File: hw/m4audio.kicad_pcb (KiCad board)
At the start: 2 copper layers, 49.7 x 49.7 mm, 94 parts, among them J1 JACK_TRS, J11 CONN_01X03, J2 JACK_TRS, J21 CONN_01X03, P1 CONN_01X02, P2 USB_OTG, P3 CONN_02X05, P4 CONN_01X08, P5 CONN_01X03, P6 CONN_01X04, U1 LD1117S33TR, U2 STM32F405RG, U3 AD8542, U4 WM8731, Y1 Crystal

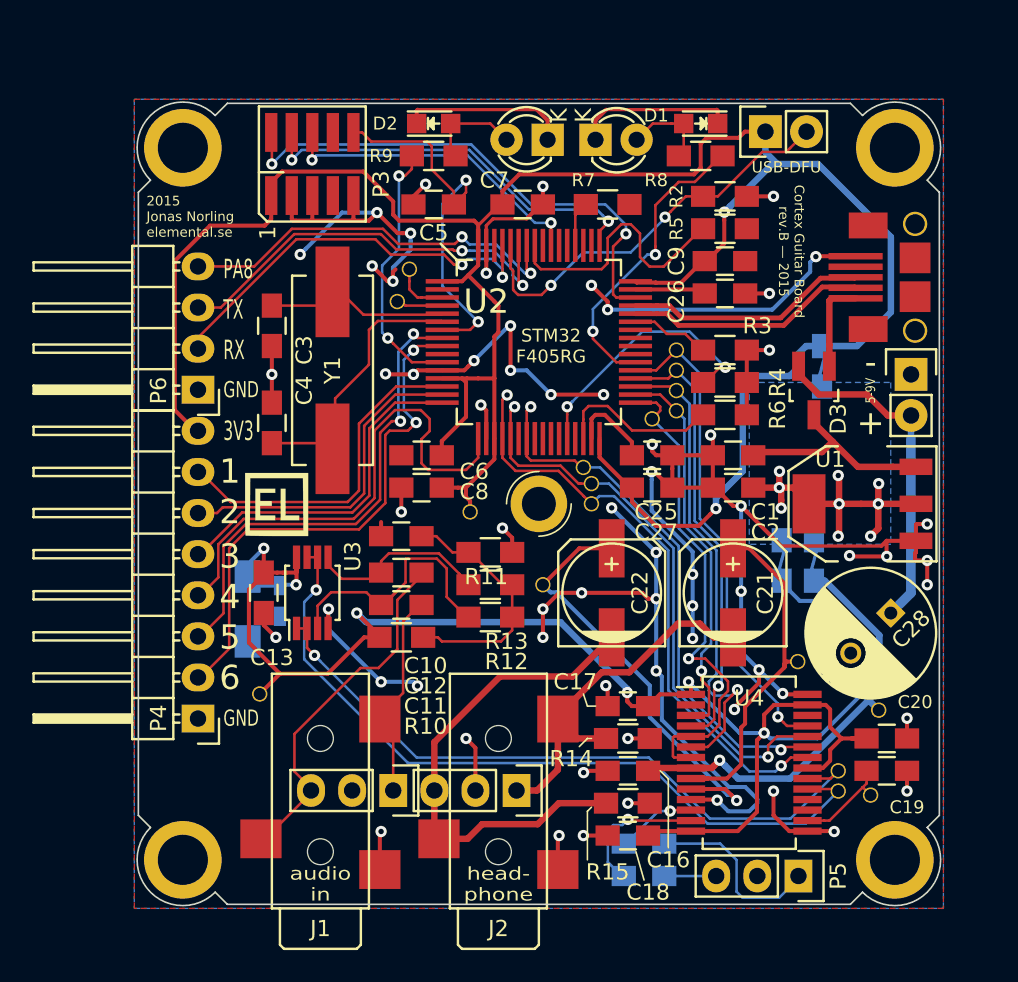
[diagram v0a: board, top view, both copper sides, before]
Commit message: Adjust testpoint drill and annular, for ITEAD production
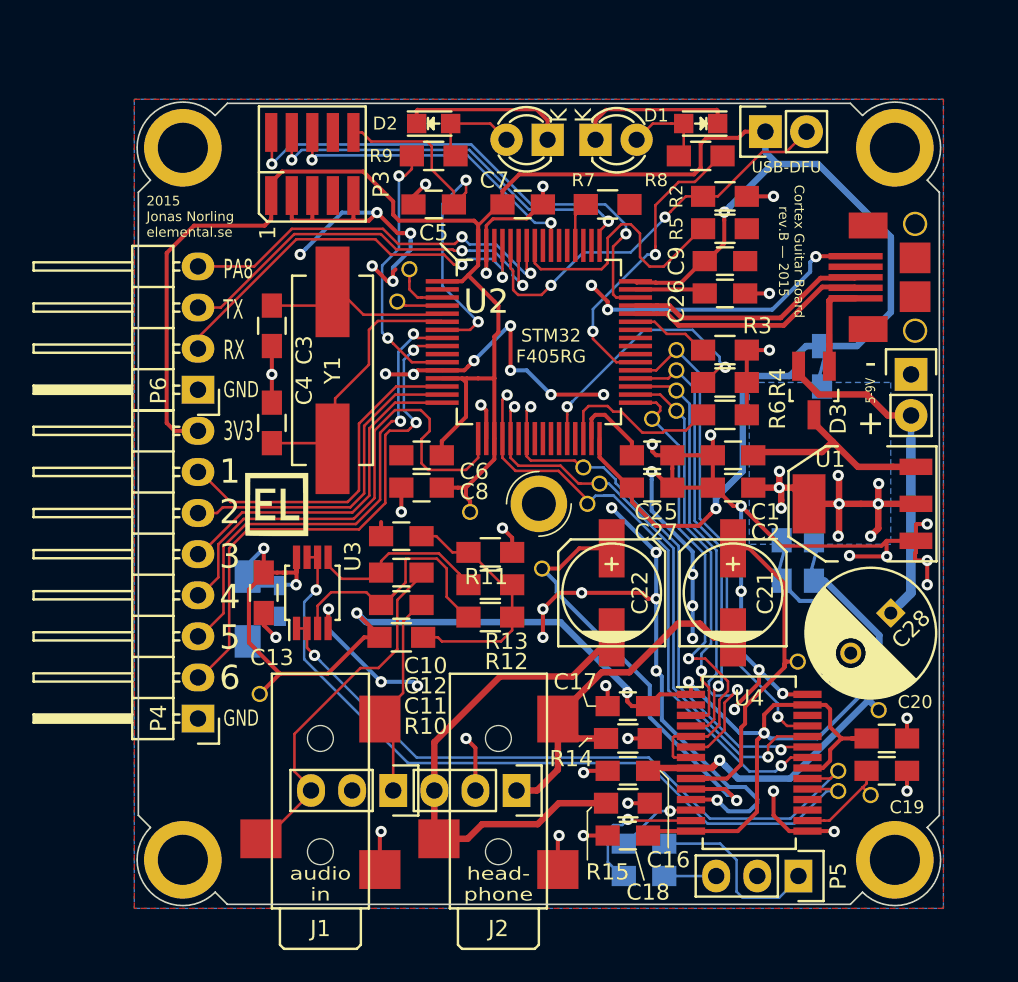
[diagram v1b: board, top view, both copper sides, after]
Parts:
- moved TP16 1.00 mm to (136.2, 119.0)
- moved TP12 0.50 mm to (139.8, 113.8)
- moved TP10 0.25 mm to (139.0, 115.0)
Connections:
- net Net-(C19-Pad2) renamed /audio/VMID
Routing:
- net VDD: track 148.2 -> 149.9 mm
- net /audio/CS: track 36.7 -> 37.5 mm
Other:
- board text added: "ADC-L"
- board text added: "ADC-R"
- board text added: "DAC-L"
- board text added: "DAC-R"
- board text added: "HPVDD"
- board text added: "VAA"
- board text added: "VMID"

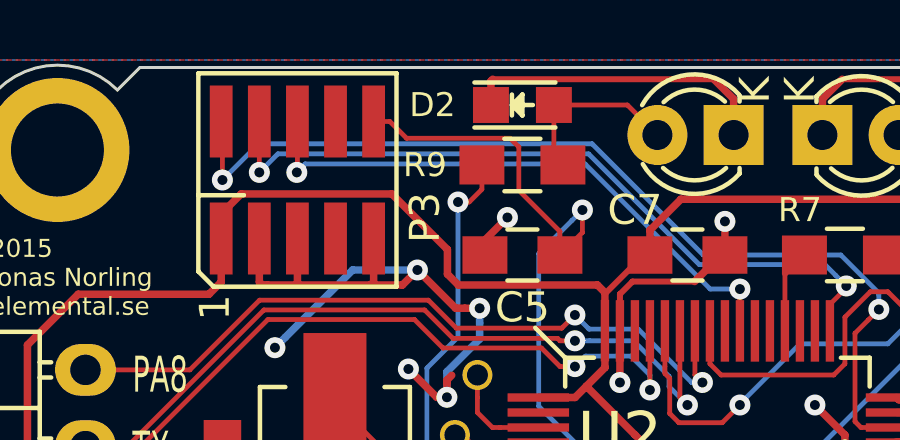
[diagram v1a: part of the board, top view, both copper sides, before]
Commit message: Add RST test point
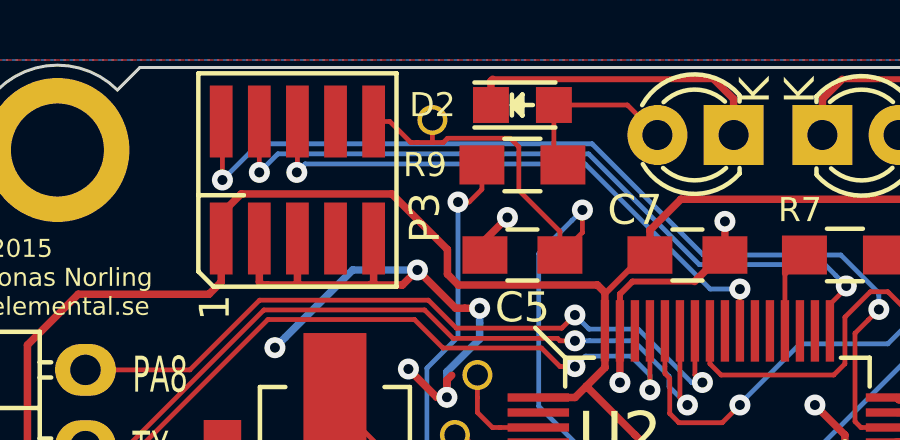
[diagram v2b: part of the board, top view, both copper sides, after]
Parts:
- added TP19: TST, Jonas_Connectors:TP_0.7mm, B.Cu at (126.5, 92.0)
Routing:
- net /NRST: track 23.9 -> 24.7 mm
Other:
- board text added: "RST"
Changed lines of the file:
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@@
 (kicad_pcb (version 4) (host pcbnew 4.0.2-2.fc24-product)
   (general
-    (links 183)
-    (no_connects 0)
-    (area 97.100001 80.8 164.687382 146.700001)
+    (links 184)
+    (no_connects 1)
+    (area 111.121572 90.121572 160.878428 139.878428)
     (thickness 1.6)
-    (drawings 120)
-    (tracks 1110)
+    (drawings 122)
+    (tracks 1115)
     (zones 0)
-    (modules 94)
+    (modules 95)
     (nets 89)
   )
@@
       (net 33 /audio/MOSI) (solder_mask_margin 0.01))
   )
+  (module Jonas_Connectors:TP_0.7mm (layer B.Cu)
+    (at 126.5 92 180)
+    (fp_text reference TP19 (at 2.1 0 180) (layer B.SilkS)
+      (effects (font (size 0.6 0.6) (thickness 0.1)) (justify mirror))
+    )
+    (fp_text value TST (at 0.25 1.25 180) (layer B.Fab) hide
+      (effects (font (size 1 1) (thickness 0.15)) (justify mirror))
+    )
+    (fp_line (start 0.5 0) (end 0.9 0) (layer B.SilkS) (width 0.15))
+    (fp_line (start 0.9 0.5) (end 0.9 -0.5) (layer B.SilkS) (width 0.15))
+    (pad 1 thru_hole circle (at 0 0 180) (size 1 1) (drill 0.7) (layers *.Cu *.Mask)
+      (net 8 /NRST) (solder_mask_margin 0.01))
+  )
+  (gr_line (start 127.25 91.5) (end 128.5 91.5) (layer B.SilkS) (width 0.1))
+  (gr_text RST (at 127.25 92) (layer B.SilkS)
+    (effects (font (size 0.5 0.5) (thickness 0.1)) (justify right mirror))
+  )
   (gr_text VMID (at 155.75 134) (layer B.SilkS)
     (effects (font (size 0.5 0.5) (thickness 0.1)) (justify right mirror))
@@
   (segment (start 121.92 132.8674) (end 119.0874 135.7) (width 0.16) (layer F.Cu) (net 7))
   (segment (start 124.54 92.05) (end 125.08 92.05) (width 0.16) (layer F.Cu) (net 8))
-  (segment (start 125.08 92.05) (end 125.639999 92.609999) (width 0.16) (layer F.Cu) (net 8))
-  (segment (start 125.639999 92.609999) (end 129.092001 92.609999) (width 0.16) (layer F.Cu) (net 8))
+  (segment (start 125.08 92.05) (end 125.78 92.75) (width 0.16) (layer F.Cu) (net 8))
+  (segment (start 125.78 92.75) (end 126 92.75) (width 0.16) (layer F.Cu) (net 8))
+  (segment (start 126 92.75) (end 126.5 92.75) (width 0.16) (layer F.Cu) (net 8))
+  (segment (start 126.5 92.75) (end 126.859999 92.75) (width 0.16) (layer F.Cu) (net 8))
+  (segment (start 126.5 92) (end 126.5 92.75) (width 0.16) (layer F.Cu) (net 8))
+  (segment (start 127 92.609999) (end 129.092001 92.609999) (width 0.16) (layer F.Cu) (net 8))
+  (segment (start 126.859999 92.75) (end 127 92.609999) (width 0.16) (layer F.Cu) (net 8))
   (segment (start 129.092001 92.609999) (end 129.380905 92.898903) (width 0.16) (layer F.Cu) (net 8))
   (segment (start 129.380905 92.898903) (end 129.380905 94.345905) (width 0.16) (layer F.Cu) (net 8))

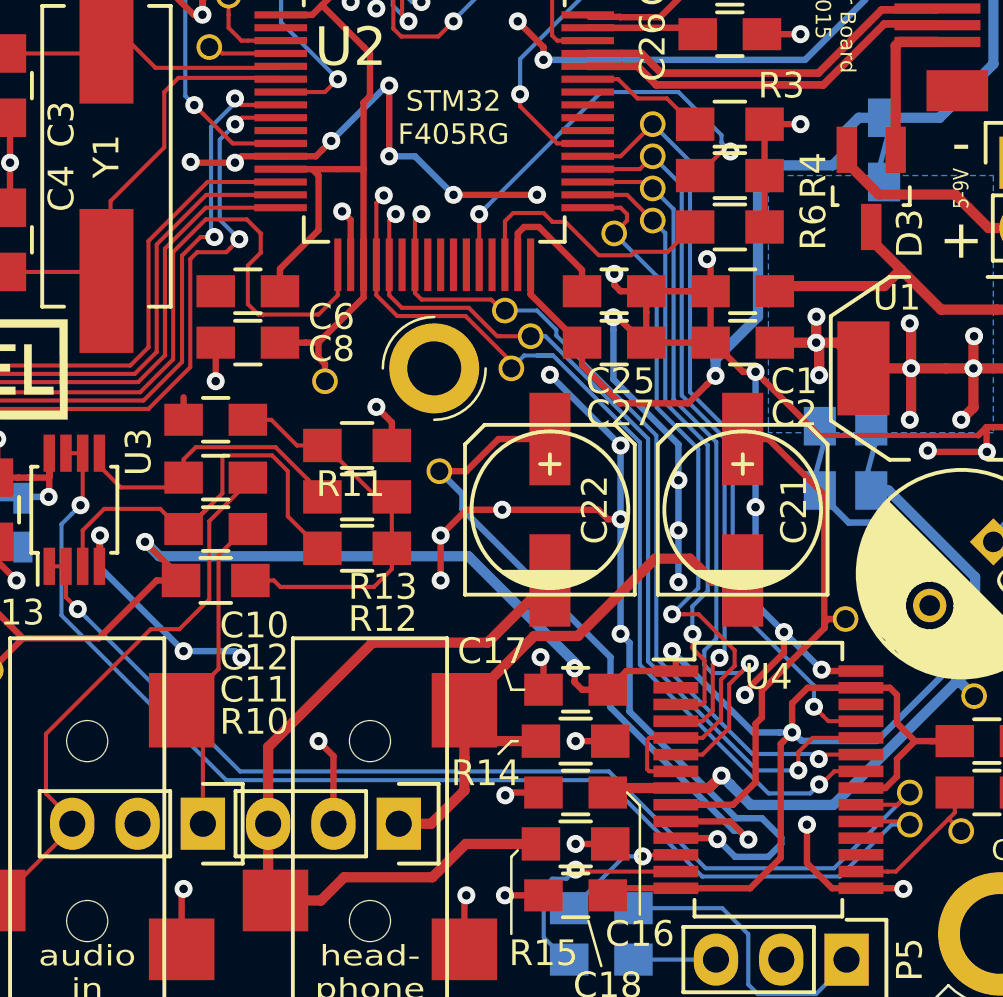
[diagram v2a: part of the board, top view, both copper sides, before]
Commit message: Use dual SMT/through hole footprint for caps
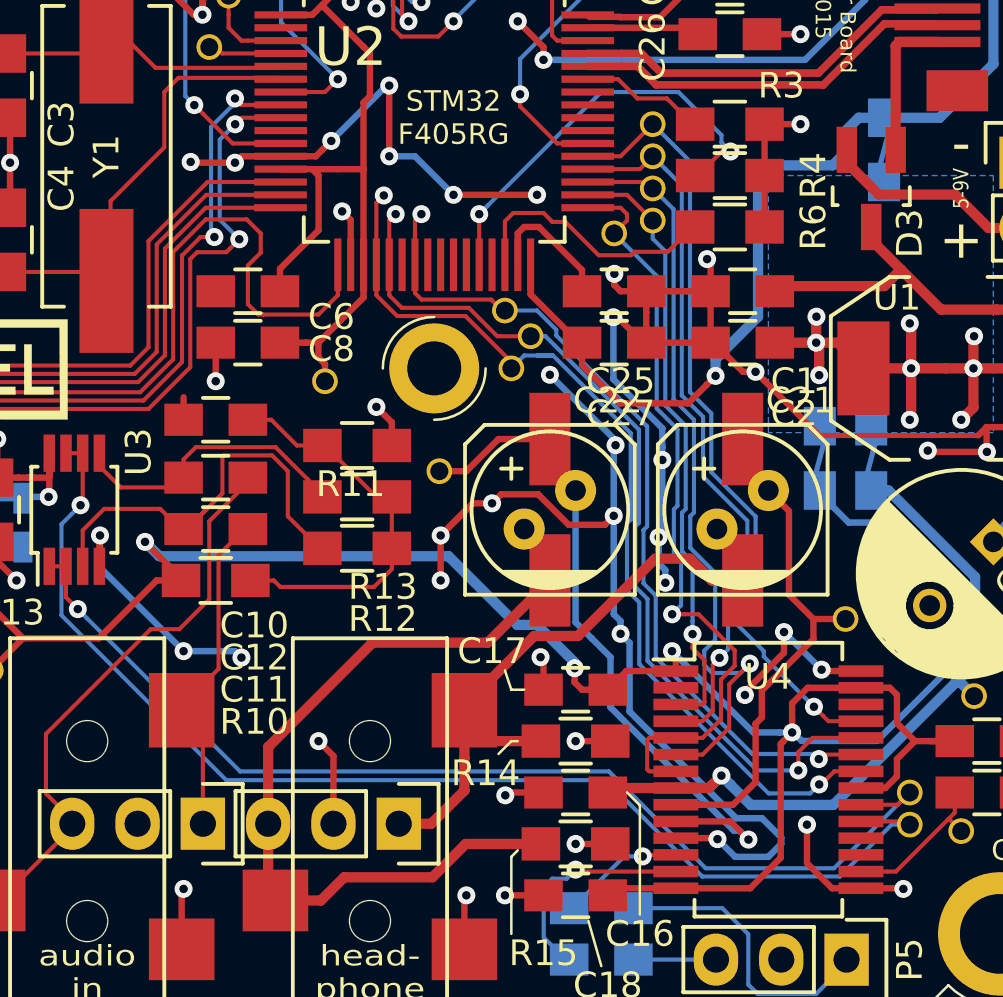
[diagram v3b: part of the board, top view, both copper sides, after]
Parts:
- C21, C22: footprint Capacitors_SMD:c_elec_6.3x7.7 -> Jonas_caps:c_elec_6.3x7.7
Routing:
- net GND: track 246.4 -> 237.5 mm, vias 65 -> 64
- net /audio/AOUT_L: track 23.4 -> 25.8 mm
- net /audio/AOUT_R: track 31.0 -> 33.4 mm
- net /audio/DACL: track 22.0 -> 21.2 mm
- net /audio/DACDAT: track 27.3 -> 28.0 mm
- net /audio/MCLK: track 30.4 -> 31.0 mm
- net /audio/DACR: track 27.6 -> 27.1 mm

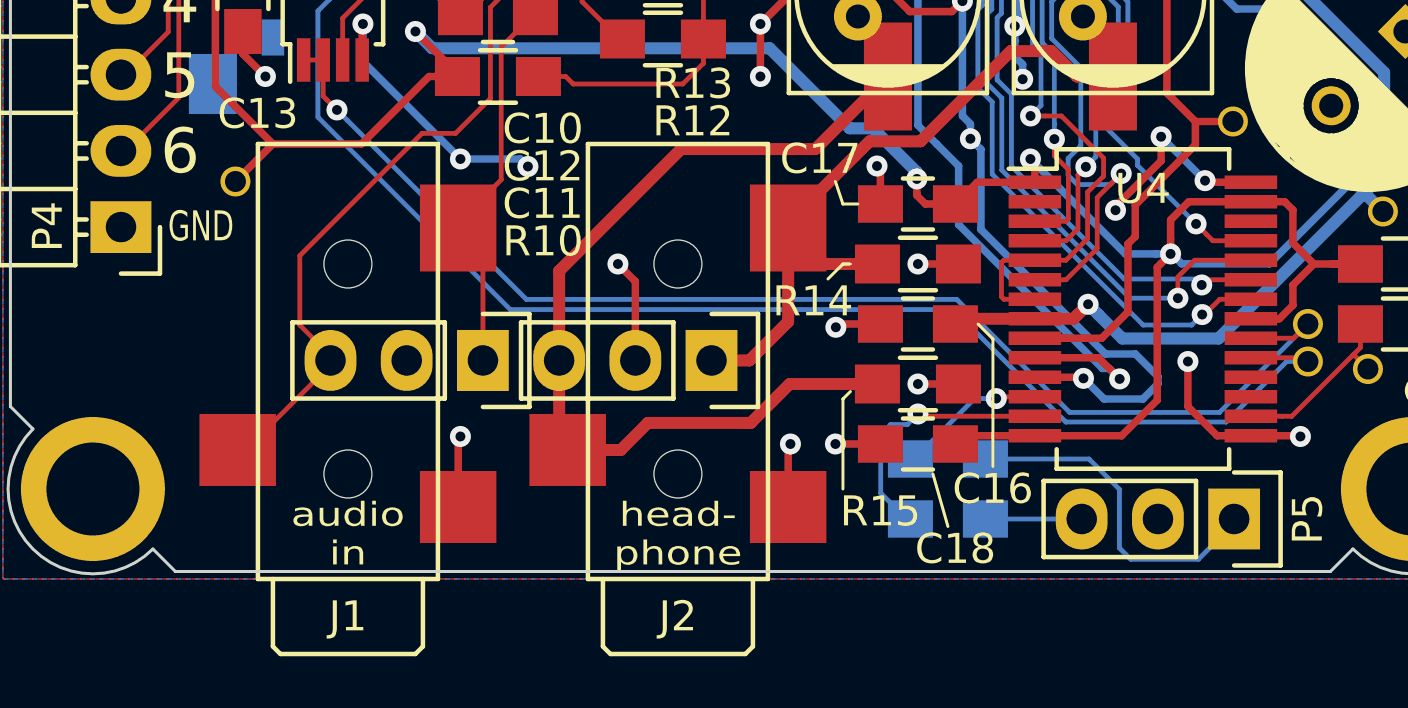
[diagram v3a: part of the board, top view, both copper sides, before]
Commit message: Silkscreen text fixes
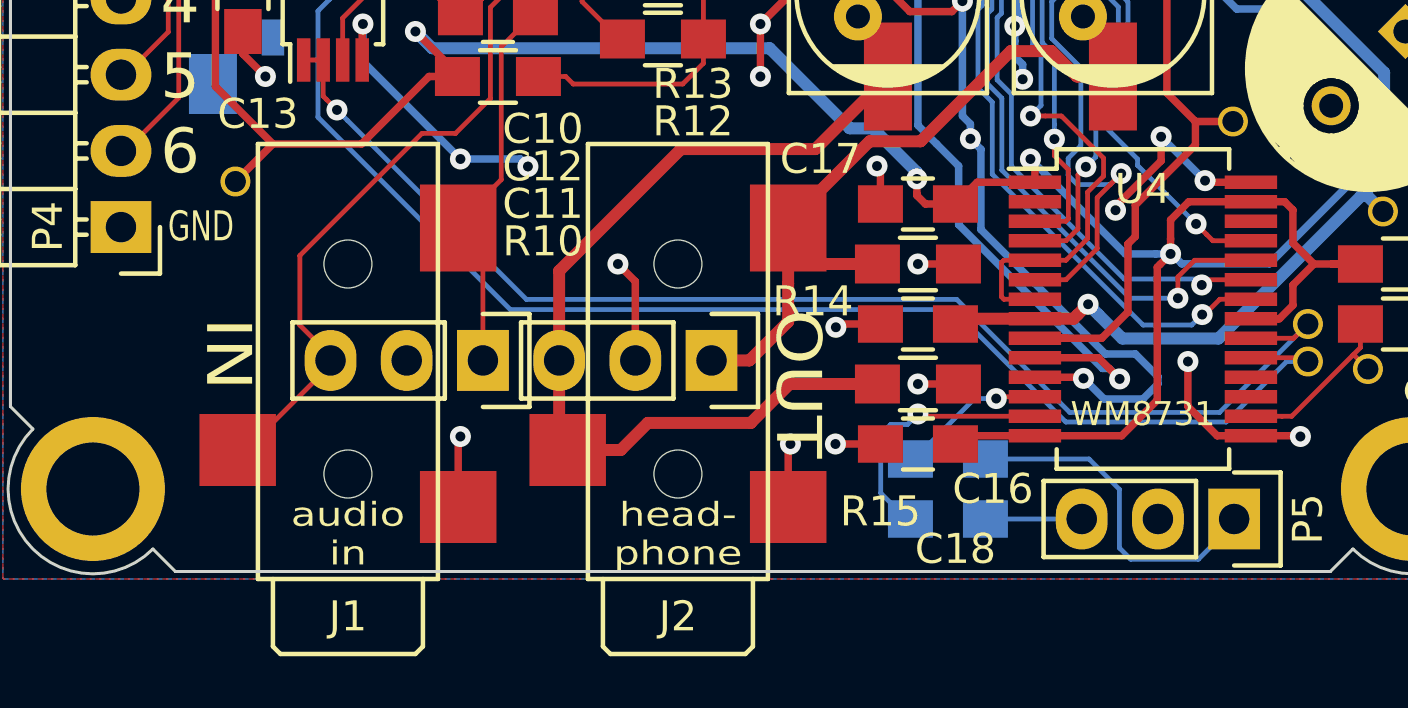
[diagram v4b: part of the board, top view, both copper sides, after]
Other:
- board text added: "WM8731"
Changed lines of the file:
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@@
     (area 111.121572 90.121572 160.878428 139.878428)
     (thickness 1.6)
-    (drawings 122)
+    (drawings 116)
     (tracks 1161)
     (zones 0)
@@
     )
   )
+  (gr_text OUT (at 137.5 133.5 270) (layer F.SilkS)
+    (effects (font (size 1.5 1.7) (thickness 0.3)))
+  )
+  (gr_text IN (at 118.5 132.5 270) (layer F.SilkS)
+    (effects (font (size 1.5 1.7) (thickness 0.3)))
+  )
+  (gr_text WM8731 (at 149 134.5) (layer F.SilkS)
+    (effects (font (size 0.8 0.8) (thickness 0.15)))
+  )
   (gr_line (start 127.25 91.5) (end 128.5 91.5) (layer B.SilkS) (width 0.1))
   (gr_text RST (at 127.25 92) (layer B.SilkS)
@@
     (effects (font (size 0.6 0.6) (thickness 0.1)) (justify mirror))
   )
-  (gr_line (start 139 127.5) (end 139.5 127.5) (layer F.SilkS) (width 0.1))
-  (gr_line (start 138.75 126.75) (end 139 127.5) (layer F.SilkS) (width 0.1))
-  (gr_line (start 139 129.5) (end 139.25 129.5) (layer F.SilkS) (width 0.1))
-  (gr_line (start 138.5 130) (end 139 129.5) (layer F.SilkS) (width 0.1))
-  (gr_line (start 139 134) (end 139.25 133.75) (layer F.SilkS) (width 0.1))
-  (gr_line (start 139 137) (end 139 134) (layer F.SilkS) (width 0.1))
-  (gr_line (start 142 136.5) (end 142.5 138.25) (layer F.SilkS) (width 0.1))
-  (gr_line (start 144 132) (end 143.5 131.5) (layer F.SilkS) (width 0.1))
-  (gr_line (start 144 136.25) (end 144 132) (layer F.SilkS) (width 0.1))
   (gr_circle (center 129.3 100.3) (end 129.55 100.3) (layer F.Mask) (width 0.3))
   (gr_text "STM32\nF405RG" (at 136.75 105.25) (layer F.SilkS)
